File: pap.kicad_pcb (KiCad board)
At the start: 2 copper layers, 43 parts, among them J1 Conn_01x02, J2 Conn_01x04, J3 Conn_01x04, J4 RJ45, J5 RJ45, J6 Conn_01x02, U1 powerstep01, Y1 32Mhz

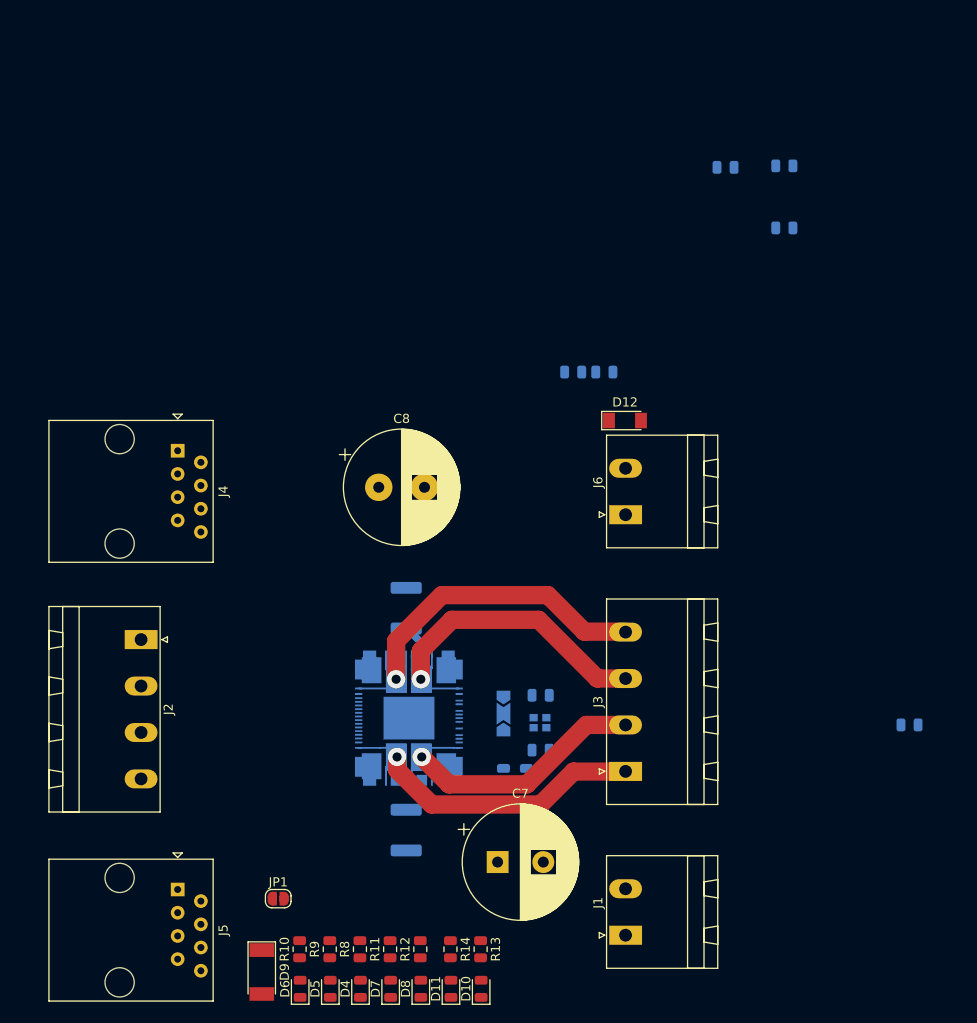
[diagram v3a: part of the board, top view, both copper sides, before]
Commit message: Cambio Rj's vuela xtal, entra Reset, agrego tornillos
Hago de todo un poco entre lo que saco el xtal porque ya probe que no se
necesita, elijo un IC que gnere 16Mhz y lo encadeno al resto, el RJ lo
cambie por otra que se parece mas a la que voy a usar, pero hay que
verificar, agregue un selector de osc, y agregue unos agujeros de
tornillos que no se si los quiero. va bien.. tengo que meterle mas al
ruteo
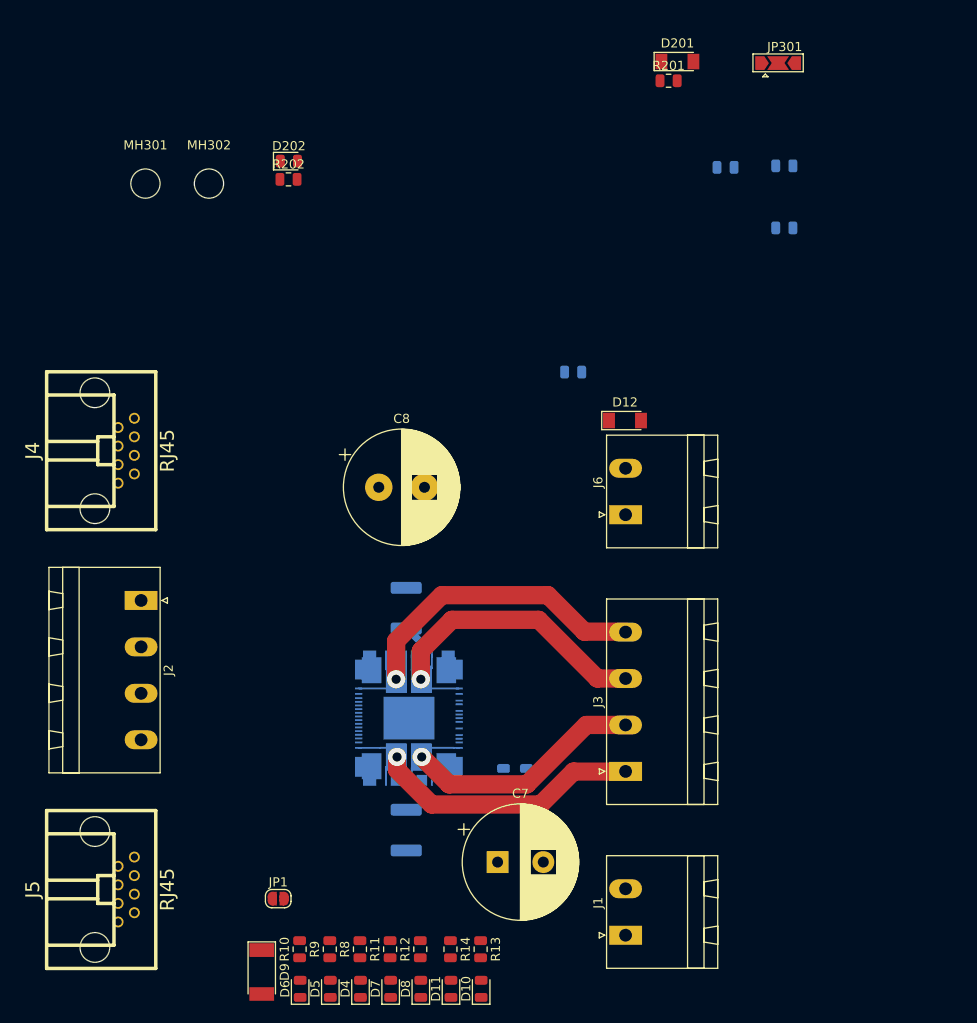
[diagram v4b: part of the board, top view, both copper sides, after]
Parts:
- removed C2, C3: 10pF, Capacitor_SMD:C_0805_2012Metric
- removed JP2: Clk_Select, Jumper:SolderJumper-3_P2.0mm_Open_TrianglePad1.0x1.5mm
- removed R1, R2: R, Resistor_SMD:R_0805_2012Metric
- removed Y1: 32Mhz, Crystal:Crystal_SMD_2016-4Pin_2.0x1.6mm
- added D201: LL4148, Diode_SMD:D_MiniMELF, F.Cu at (155.7, 46.4)
- added D202: LED, LED_SMD:LED_0805_2012Metric, F.Cu at (113.2, 57.3)
- added JP301: Clk_Select, Jumper:SolderJumper-3_P2.0mm_Open_TrianglePad1.0x1.5mm, F.Cu at (166.7, 46.6)
- added MH301: MountingHole, MountingHole:MountingHole_3.2mm_M3, F.Cu at (97.5, 59.8)
- added MH302: MountingHole, MountingHole:MountingHole_3.2mm_M3, F.Cu at (104.4, 59.8)
- added R201: R, Resistor_SMD:R_0805_2012Metric, F.Cu at (154.7, 48.5)
- added R202: R, Resistor_SMD:R_0805_2012Metric, F.Cu at (113.1, 59.3)
- J4, J5: footprint Connector_RJ:RJ45_Amphenol_54602-x08_Horizontal -> w_conn_pc:rj45-noshield
- moved J4 9.00 mm to (92.0, 89.0)
- moved J5 9.00 mm to (92.0, 137.0)
- moved J2 4.28 mm to (97.0, 105.4)
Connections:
- net Net-(C6-Pad2) renamed /motor/Adc
- J4 pad 1: /connector/CS -> G3V3
- J4 pad 2: /connector/CLK -> /connector/Busy_Out
- J4 pad 3: /connector/SDI -> /connector/Reset
- J4 pad 4: Net-(J4-Pad4) -> /connector/Osc
- J4 pad 5: /connector/CLKIN -> /connector/Sdo_Chain
- J4 pad 6: Net-(J4-Pad6) -> /connector/SDI
- J4 pad 7: Net-(J4-Pad7) -> /connector/CLK
- J4 pad 8: G3V3 -> /connector/CS
- J5 pad 2: Net-(J4-Pad7) -> /connector/Busy_Out
- J5 pad 3: Net-(J5-Pad3) -> /connector/Reset
- J5 pad 4: /connector/CLKIN -> /connector/Osc
- J5 pad 5: Net-(J4-Pad4) -> /connector/Sdo_Chain
- JP1 pad 1: /connector/Busy -> /connector/Busy_Out
- JP1 pad 2: Net-(J4-Pad7) -> /connector/Busy
- U1 pad 16: /motor/Flag -> /motor/flag
- U1 pad 18: Net-(R2-Pad1) -> /motor/Switch_Local
- U1 pad 19: /motor/Reset -> /connector/Reset
- U1 pad 63: Net-(JP2-Pad3) -> /connector/Osc_In
- U1 pad 64: Net-(C2-Pad1) -> /connector/Osc_Out

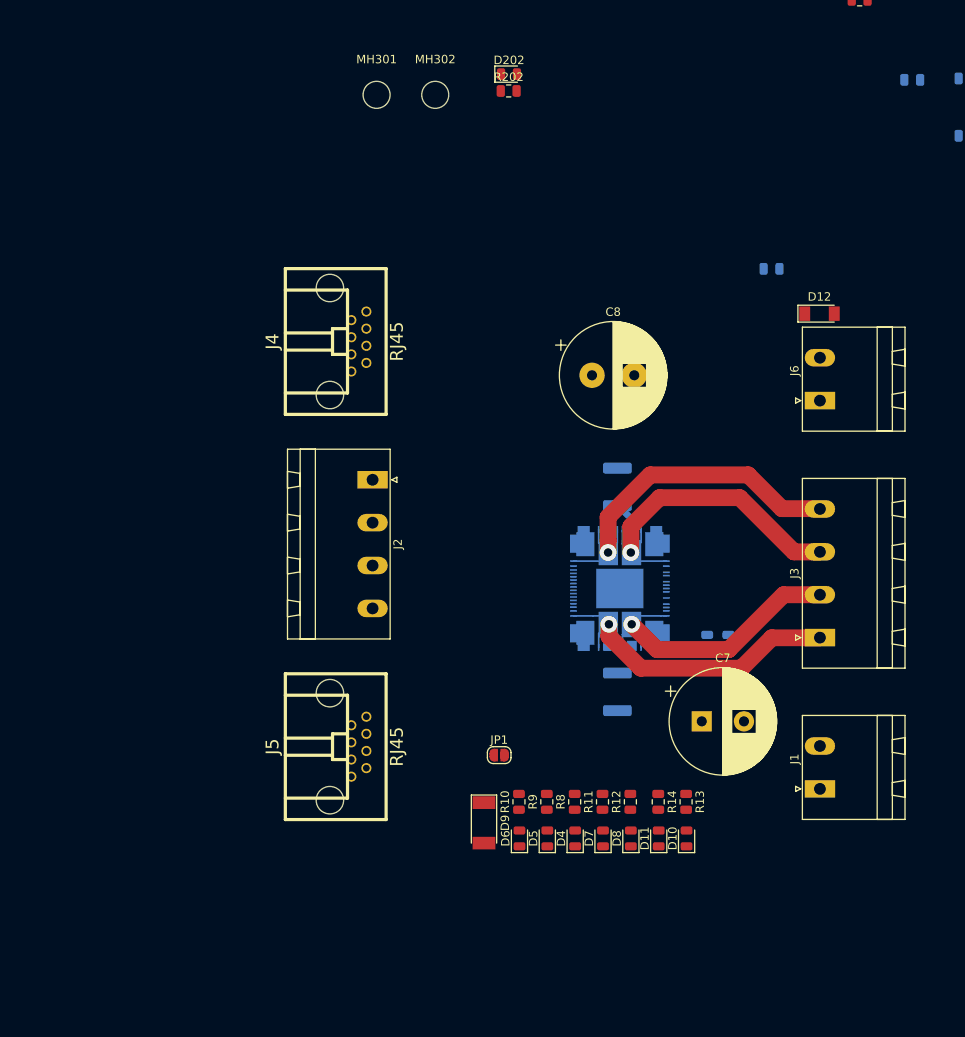
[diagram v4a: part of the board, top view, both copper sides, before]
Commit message: cambio nombres, hago board edge, defino capas, posicion y demas
hice de todo un poco, principalmente le di forma a la placa con una
dimensino pasable, ajuste los conectores que aun no me convencen, pero
cambie la entrada para el conector de 4 y los motores en 2 de 2, cosa
que la alimentacion este toda en un solo conector y me queda piola para
que los motores salgan del IC para los costados. en cuanto a la logica
aun no me decido si voy a poner otra RJ para la salida d busy y demas o
meto bornera.. estouy mas del lado de la RJ y me quedaria genial para
poner los leds arriba de la RJ o a un costado.. puedo elegir eso.. mepa
que vamos con eso y asi no hay manera de mezclar fichas tampoco, porque
pongo un 6P6C RJ12 y ya.. hasta me sobran 2 pines.. bueno despues lo
sigo.
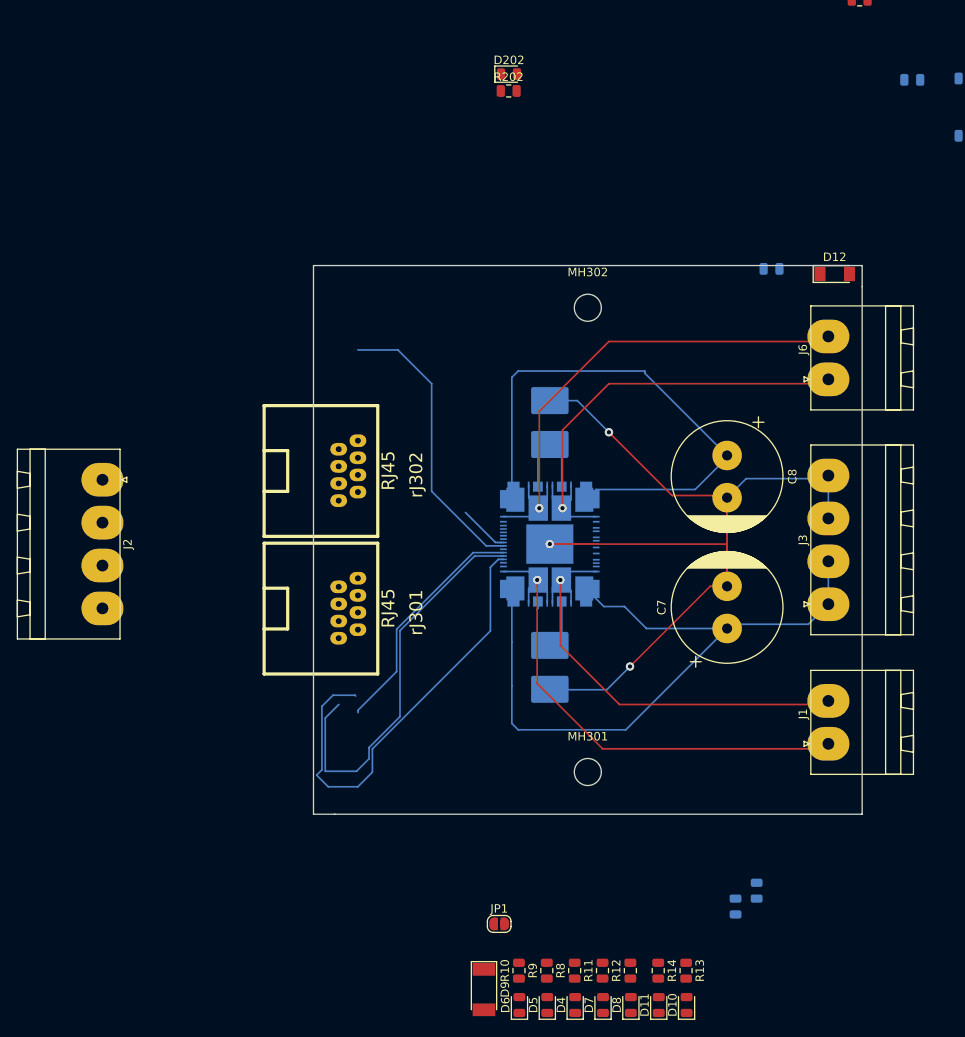
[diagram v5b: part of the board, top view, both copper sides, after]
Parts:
- removed J4, J5: RJ45, w_conn_pc:rj45-noshield
- added rJ301: RJ45, pap:rj45_dci, F.Cu at (91.0, 120.6)
- added rJ302: RJ45, powerstep:rj45_dci, F.Cu at (91.0, 104.3)
- C7, C8: footprint Capacitor_THT:CP_Radial_D12.5mm_P5.00mm -> powerstep:CP_Radial_D13.0mm_P5.00mm
- J1, J6: footprint Connector_Phoenix_MSTB:PhoenixContact_MSTBA_2,5_2-G-5,08_1x02_P5.08mm_Horizontal -> powerstep:PhoenixContact_MSTBA_2,5_2-G-5,08_1x02_P5.08mm_Horizontal
- J2, J3: footprint Connector_Phoenix_MSTB:PhoenixContact_MSTBA_2,5_4-G-5,08_1x04_P5.08mm_Horizontal -> powerstep:PhoenixContact_MSTBA_2,5_4-G-5,08_1x04_P5.08mm_Horizontal
- R3, R4: footprint Resistor_SMD:R_1812_4532Metric_Pad1.30x3.40mm_HandSolder -> Resistor_SMD:R_2816_7142Metric_Pad3.20x4.45mm_HandSolder
- U1: footprint powerstep:powerstep -> pap:powerstep
- moved MH301 84.0 mm to (122.5, 140.0)
- moved J2 32.0 mm to (65.0, 105.4)
- moved C4 31.4 mm to (140.0, 155.9)
- moved MH302 31.0 mm to (122.5, 85.0)
- moved C6 29.6 mm to (142.5, 154.1)
- moved JP1 20.0 mm to (112.0, 158.0)
- moved R10 20.0 mm to (114.3, 163.5)
- moved R11 20.0 mm to (124.2, 163.5)
- moved R12 20.0 mm to (127.5, 163.5)
- moved R13 20.0 mm to (134.1, 163.5)
- moved R14 20.0 mm to (130.8, 163.5)
- moved R8 20.0 mm to (120.9, 163.5)
- moved R9 20.0 mm to (117.6, 163.5)
- moved D10 19.7 mm to (134.2, 167.6)
- moved D11 19.7 mm to (130.9, 167.6)
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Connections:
- J1 pad 1: 85v -> /connector/MotorB2
- J1 pad 2: 85v -> /connector/MotorB1
- J2 pad 1: Net-(J2-Pad1) -> G3V3
- J3 pad 1: /connector/MotorB2 -> 85v
- J3 pad 2: /connector/MotorB1 -> 85v
- J3 pad 3: /connector/MotorA1 -> G85V
- J3 pad 4: /connector/MotorA2 -> G85V
- J6 pad 1: G85V -> /connector/MotorA1
- J6 pad 2: G85V -> /connector/MotorA2
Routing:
- net 85v: track 0.00 -> 146.1 mm
- net G85V: track 0.00 -> 122.8 mm, vias 0 -> 3
- net /connector/CS: track 0.00 -> 52.9 mm
- net /connector/CLK: track 0.00 -> 47.0 mm
- net /connector/SDO: track 0.00 -> 34.3 mm
- net /connector/SDI: track 0.00 -> 28.1 mm
- net /connector/MotorB2: track 40.5 -> 61.2 mm
- net /connector/MotorA2: track 42.4 -> 60.4 mm
- net /connector/MotorB1: track 37.5 -> 53.6 mm
- net /connector/MotorA1: track 40.6 -> 54.0 mm
- net Net-(R3-Pad1): track 0.00 -> 11.6 mm
- net /connector/Busy: track 0.00 -> 5.97 mm
- net Net-(R4-Pad1): track 7.08 -> 11.1 mm
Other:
- board outline added: 65 x 65 mm

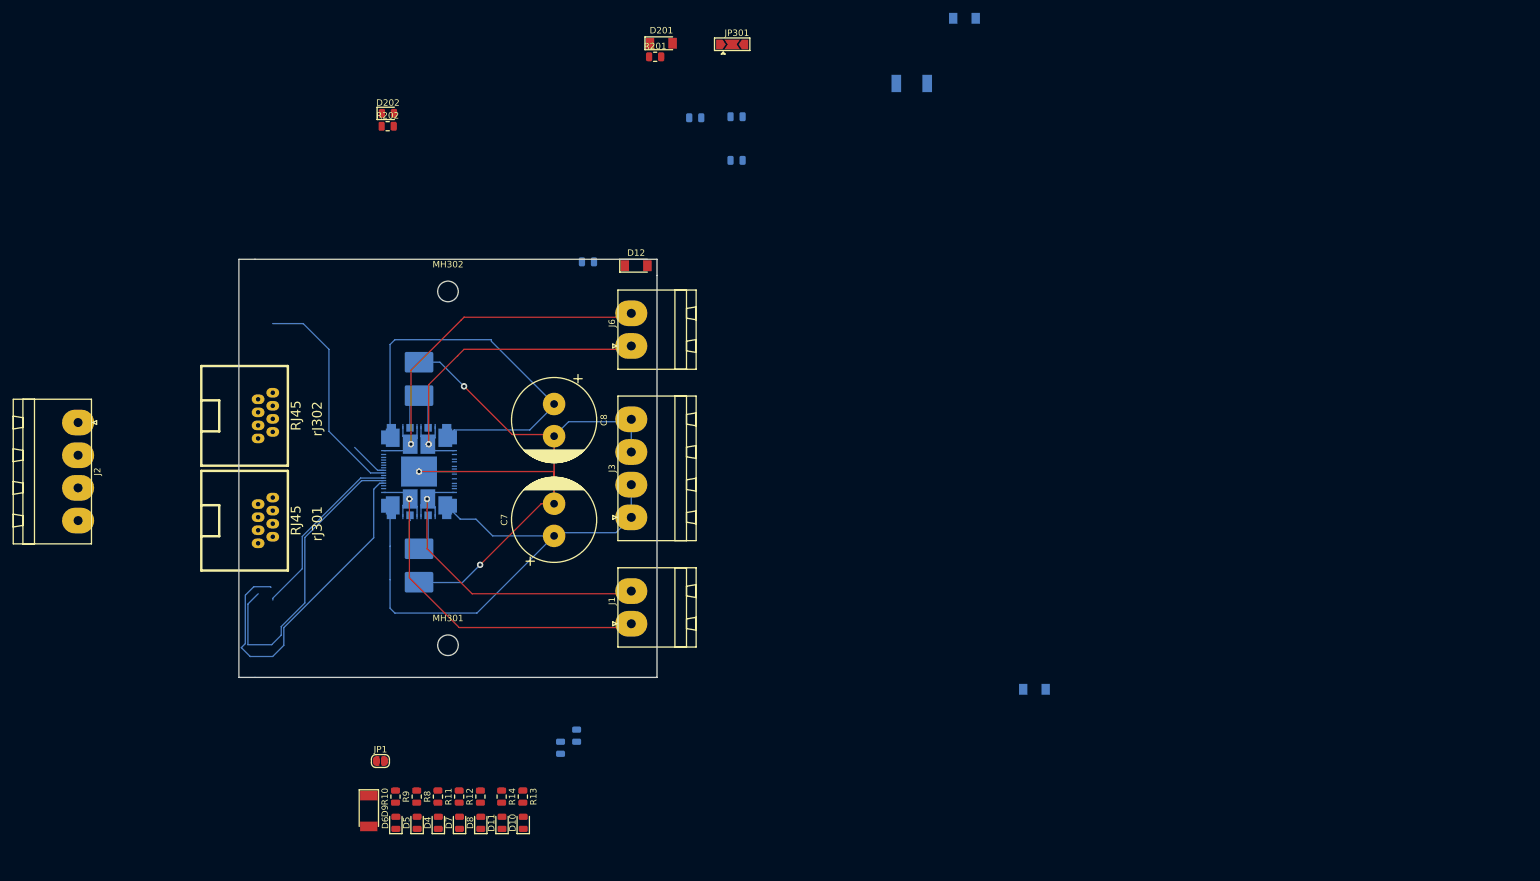
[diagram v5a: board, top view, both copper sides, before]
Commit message: achico placa, agrego rj12, defino pistas, ruteo potencia
ahi le voy dando forma. ya rute la potencia y esta mas o menios bien,
ahora estoy viendo el tema de los leds para ponmerlos encima de los
conectores con patas porque es la mejor opcion que se me ocurrio y ya la
tengo probada.. con leds SMD despues tengo que hacer un chino para
sacarlo para afuera y de costado necesito acrilico puro para conducir..
es mas laburo.. con patas hago 2x1.. veremos como queda
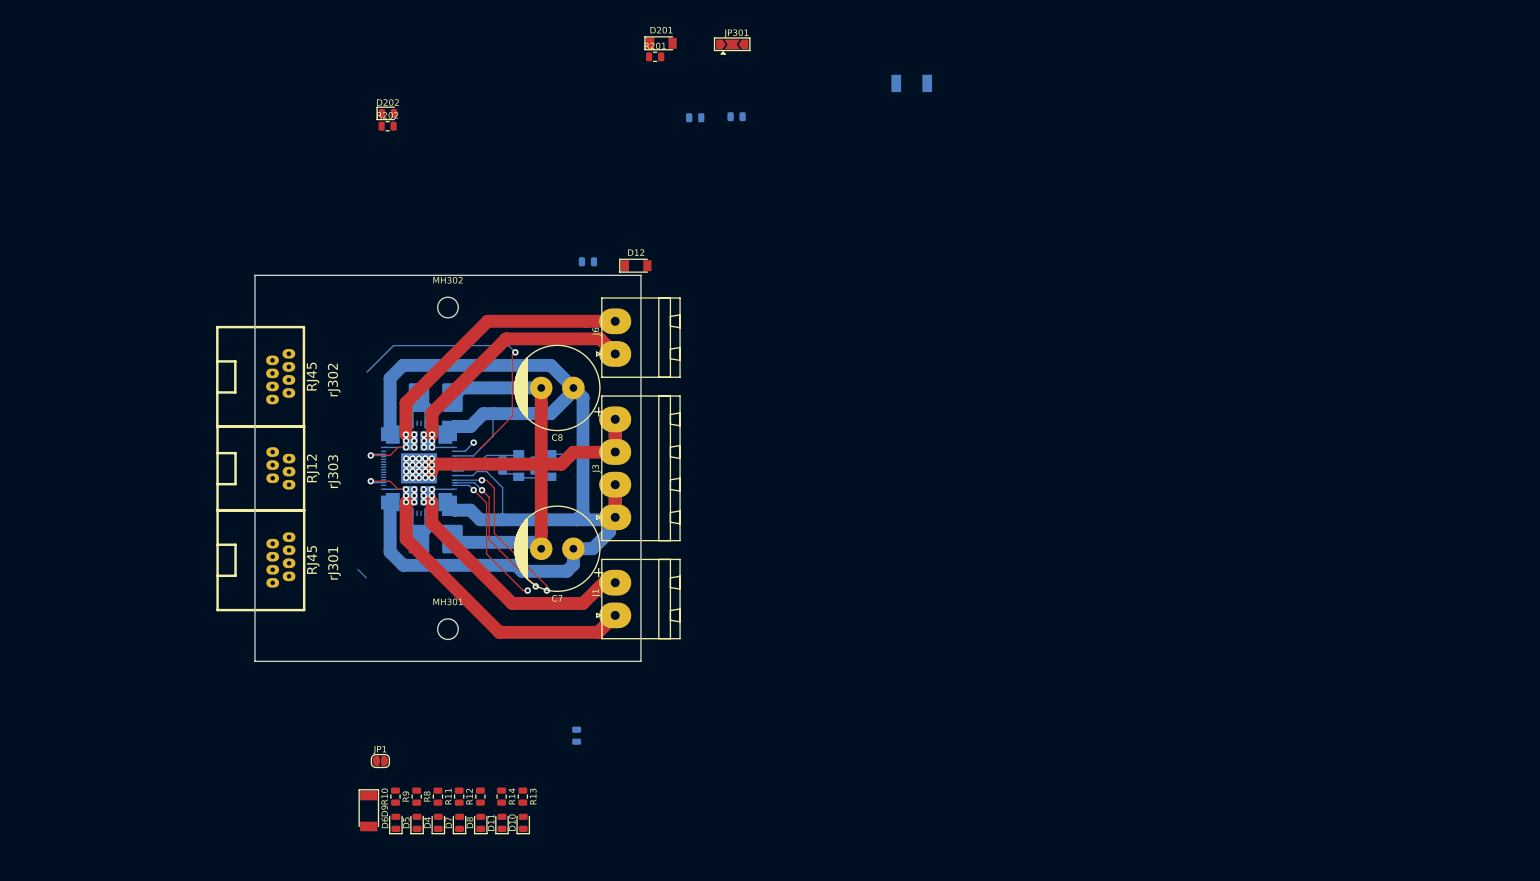
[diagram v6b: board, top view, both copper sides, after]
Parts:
- removed J2: Conn_01x04, powerstep:PhoenixContact_MSTBA_2,5_4-G-5,08_1x04_P5.08mm_Horizontal
- added rJ303: RJ12, pap:rj12, F.Cu at (93.5, 112.5)
- C7, C8: footprint powerstep:CP_Radial_D13.0mm_P5.00mm -> pap:CP_Radial_D13.0mm_P5.00mm
- J1, J6: footprint powerstep:PhoenixContact_MSTBA_2,5_2-G-5,08_1x02_P5.08mm_Horizontal -> pap:PhoenixContact_MSTBA_2,5_2-G-5,08_1x02_P5.08mm_Horizontal
- J3: footprint powerstep:PhoenixContact_MSTBA_2,5_4-G-5,08_1x04_P5.08mm_Horizontal -> pap:PhoenixContact_MSTBA_2,5_4-G-5,08_1x04_P5.08mm_Horizontal
- rJ301: footprint pap:rj45_dci -> pap:rj45
- rJ302: footprint powerstep:rj45_dci -> pap:rj45
- moved D2 98.2 mm to (133.5, 112.1), turned to 270 degrees
- moved D3 82.8 mm to (138.5, 112.1), turned to 90 degrees
- moved C5 59.8 mm to (131.0, 112.1), turned to 270 degrees
- moved C4 44.1 mm to (136.0, 112.1)
- moved rJ301 6.65 mm to (93.5, 126.8)
- moved rJ302 6.55 mm to (93.5, 98.2)
- moved R3 4.85 mm to (120.6, 123.5), turned to 0 degrees
- moved C8 3.91 mm to (142.0, 100.0), turned to 180 degrees
- moved R4 3.89 mm to (120.6, 101.5), turned to 0 degrees
- moved C7 3.61 mm to (142.0, 125.0), turned to 180 degrees
- moved J1 2.82 mm to (148.5, 135.4)
- moved J6 2.79 mm to (148.5, 94.7)
- moved J3 2.50 mm to (148.5, 120.1)
- moved MH301 2.50 mm to (122.5, 137.5)
- moved MH302 2.50 mm to (122.5, 87.5)
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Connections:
- net Net-(C4-Pad1) renamed /motor/Vboot
- net Net-(C5-Pad1) renamed /motor/Cpump
- net Net-(R3-Pad1) renamed /motor/SenseB
- net Net-(R4-Pad1) renamed /motor/SenseA
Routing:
- net 85v: track 146.1 -> 202.7 mm
- net /connector/CS: track 52.9 -> 0.00 mm
- net /connector/CLK: track 47.0 -> 0.00 mm
- net /motor/Adc: track 0.00 -> 46.1 mm, vias 0 -> 2
- net /connector/SDO: track 34.3 -> 0.00 mm
- net /connector/SDI: track 28.1 -> 0.00 mm
- net 3v3: track 0.00 -> 26.0 mm, vias 0 -> 2
- net /connector/Osc_Out: track 0.00 -> 24.6 mm, vias 0 -> 2
- net G85V: track 122.8 -> 99.4 mm, vias 3 -> 20
- net /connector/Osc_In: track 0.00 -> 23.2 mm, vias 0 -> 2
- net /motor/Vboot: track 0.00 -> 13.7 mm
- net /connector/MotorA1: track 54.0 -> 41.2 mm, vias 1 -> 6
- net /connector/MotorB1: track 53.6 -> 41.8 mm, vias 1 -> 6
- net /connector/MotorA2: track 60.4 -> 52.2 mm, vias 1 -> 6
- net Net-(C5-Pad2): track 0.00 -> 7.76 mm
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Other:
- board size 65 x 65 mm -> 60 x 60 mm
- net class HV added: clearance 1, trace_width 2, via_dia 1, via_drill 0.5
- net class Mid_Power added: clearance 0.4, trace_width 0.8, via_dia 1.2, via_drill 0.6
- net class Power added: clearance 0.6, trace_width 1, via_dia 1.6, via_drill 1
- net class Sense added: clearance 0.2, trace_width 1.15, via_dia 1, via_drill 0.5
